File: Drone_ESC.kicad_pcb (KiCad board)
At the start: 2 copper layers, 62 parts, among them IC1 DRV8323RSRGZR, J1 Input, J2 62701021621, Q1 BSC014N06NS, Q2 BSC014N06NS, Q3 BSC014N06NS, Q4 BSC014N06NS, Q5 BSC014N06NS, Q6 BSC014N06NS, SW1 Reset, U1 STM32G473RCTx, Y1 XRCGB24M000F3A00R0

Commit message: Update Drone_ESC.kicad_pcb
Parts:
- C1, C10, C11, C12, C2, C21, C23, C24, C25, C26, C27, C28, C29, C3, C30, C31, C32, C4, C5, C6, C7, C8, C9, D1, IC1, R15, R16, U1: moved to B.Cu
- moved J2 147.4 mm to (130.9, 55.3)
- moved U1 135.9 mm to (142.5, 67.5), turned to 180 degrees
- moved R11 134.4 mm to (167.0, 67.5), turned to 180 degrees
- moved L1 131.0 mm to (142.1, 85.2)
- moved R12 130.4 mm to (167.0, 79.5), turned to 180 degrees
- moved IC1 129.8 mm to (153.0, 86.0), turned to -90 degrees
- moved D1 129.3 mm to (145.1, 85.8), turned to -90 degrees
- moved C5 128.2 mm to (132.3, 63.3), turned to -90 degrees
- moved C6 128.0 mm to (134.5, 63.3), turned to -90 degrees
- moved R13 126.6 mm to (167.0, 91.5), turned to 180 degrees
- moved C8 124.9 mm to (146.7, 59.5), turned to 180 degrees
- moved C7 124.5 mm to (146.7, 57.5), turned to 180 degrees
- moved R15 122.0 mm to (149.0, 77.8), turned to -90 degrees
- moved R16 121.8 mm to (151.0, 77.8), turned to 90 degrees
- moved C32 121.4 mm to (138.1, 83.0), turned to 90 degrees
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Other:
- copper layers 2 -> 6
- board text added: "1. Top: Main motor currents 2. GND 3. Critical Signals 4. 3.3V 5. Logic and BEMF 6. Leftover decoupling caps & GND pour"

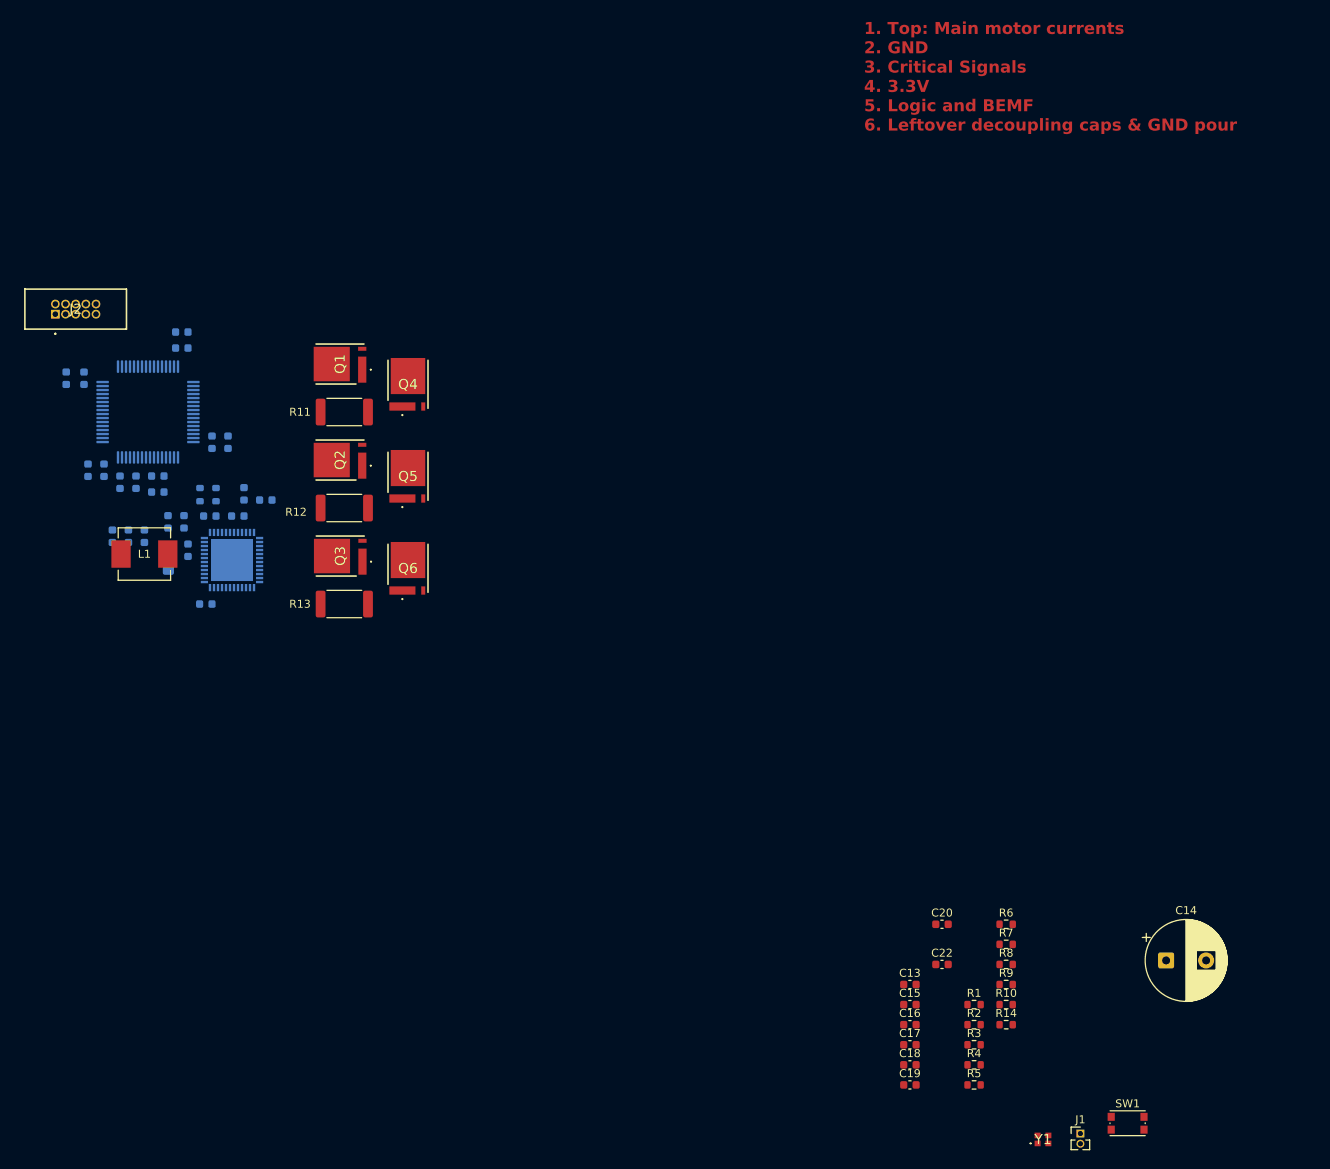
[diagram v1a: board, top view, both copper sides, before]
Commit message: PCB layout done, wiring next
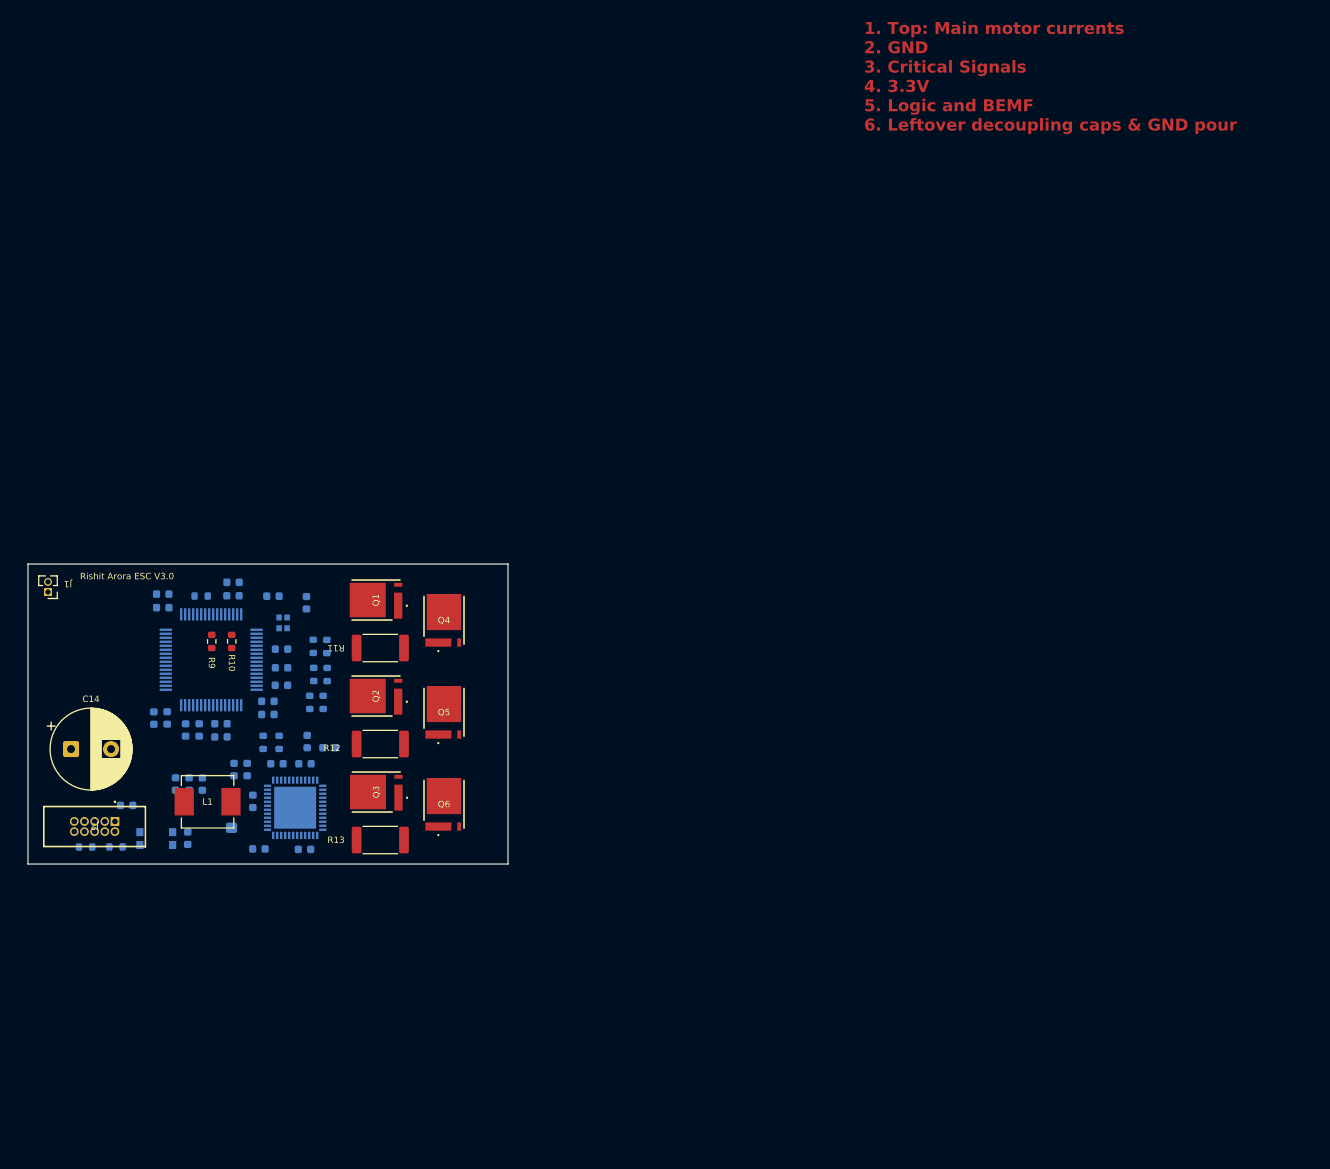
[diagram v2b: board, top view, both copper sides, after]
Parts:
- C13, C15, C16, C17, C18, C19, C20, C22, R1, R14, R2, R3, R4, R5, R6, R7, R8, SW1, Y1: moved to B.Cu
- moved J1 145.7 mm to (130.0, 90.0), turned to 180 degrees
- moved C14 139.4 mm to (132.9, 109.6)
- moved SW1 126.5 mm to (143.5, 120.8), turned to 180 degrees
- moved Y1 114.9 mm to (159.4, 93.9), turned to -90 degrees
- moved R14 114.0 mm to (149.1, 90.5), turned to 180 degrees
- moved R2 113.3 mm to (134.7, 121.9), turned to 180 degrees
- moved R1 109.1 mm to (138.5, 121.9), turned to 180 degrees
- moved R9 108.2 mm to (150.5, 96.2), turned to -90 degrees
- moved R10 106.9 mm to (153.0, 96.2), turned to -90 degrees
- moved C13 100.4 mm to (139.8, 116.7), turned to 180 degrees
- moved R3 95.0 mm to (164.9, 96.8), turned to 90 degrees
- moved R4 94.4 mm to (164.9, 100.3), turned to -90 degrees
- moved R5 94.4 mm to (164.4, 103.8), turned to -90 degrees
- moved R6 93.3 mm to (163.2, 96.8), turned to -90 degrees
- moved C20 93.1 mm to (158.1, 90.5)
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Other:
- board outline added: 60 x 37.5 mm
- board text added: "Rishit Arora ESC V3.0"

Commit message: Almost done with routing
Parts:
- moved C14 3.99 mm to (135.0, 106.2), turned to -90 degrees
- moved C22 1.74 mm to (163.8, 122.2)
- moved R9 1.56 mm to (151.7, 97.1)
- moved Q1 1.50 mm to (172.5, 91.0)
- moved Q2 1.50 mm to (172.5, 103.0)
- moved Q3 1.50 mm to (172.5, 115.0)
- moved Q4 1.50 mm to (181.0, 93.5)
- moved Q5 1.50 mm to (181.0, 105.0)
- moved Q6 1.50 mm to (181.0, 116.5)
- moved R11 1.50 mm to (173.0, 97.0)
- moved R12 1.50 mm to (173.0, 109.0)
- moved R13 1.50 mm to (173.0, 121.0)
- moved C28 1.24 mm to (161.7, 110.3)
- moved R10 1.19 mm to (154.1, 95.8)
- moved C24 0.82 mm to (155.3, 115.4)
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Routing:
- net RESET: track 0.00 -> 97.7 mm, vias 0 -> 2
- net GND: track 0.00 -> 96.2 mm, vias 0 -> 46
- net FAULT: track 0.00 -> 55.0 mm, vias 0 -> 3
- net +3.3V: track 0.00 -> 49.5 mm, vias 0 -> 16
- net SWO: track 0.00 -> 46.9 mm, vias 0 -> 1
- net SDO: track 0.00 -> 45.6 mm, vias 0 -> 2
- net DRIVER_EN: track 0.00 -> 43.0 mm, vias 0 -> 2
- net NSCS: track 0.00 -> 41.6 mm, vias 0 -> 2
- net SDI: track 0.00 -> 39.6 mm, vias 0 -> 2
- net SCLK: track 0.00 -> 39.0 mm, vias 0 -> 2
- net INHA: track 0.00 -> 37.9 mm, vias 0 -> 2
- net SWDCLK: track 0.00 -> 37.8 mm, vias 0 -> 1
- net INLA: track 0.00 -> 34.8 mm, vias 0 -> 2
- net INHC: track 0.00 -> 34.5 mm, vias 0 -> 2
- net INHB: track 0.00 -> 34.4 mm, vias 0 -> 2
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- added copper zone on B.Cu, net +3.3V
- added copper zone on F.Cu, net +3.3V
- added copper zone on In3.Cu, net +3.3V
- added copper zone on B.Cu, net +BATT
- added copper zone on F.Cu, net +BATT
- added copper zone on F.Cu, net GHA
- added copper zone on In2.Cu, net GHA
- added copper zone on F.Cu, net GHB
- added copper zone on In2.Cu, net GHB
- added copper zone on F.Cu, net GHC
- added copper zone on In2.Cu, net GHC
- added copper zone on F.Cu, net GLA
- added copper zone on In2.Cu, net GLA
- added copper zone on F.Cu, net GLB
- added copper zone on In2.Cu, net GLB
- added copper zone on F.Cu, net GLC
- added copper zone on In2.Cu, net GLC
- added copper zone on B.Cu, net GND
- added copper zone on In1.Cu, net GND
- added copper zone on B.Cu, net Net-(D1-K)
- added copper zone on B.Cu, net Net-(IC1-FB)
- added copper zone on F.Cu, net PHASE_A
- added copper zone on F.Cu, net PHASE_B
- added copper zone on F.Cu, net PHASE_C
- added copper zone on F.Cu, net SENSE_A
- added copper zone on F.Cu, net SENSE_B
- added copper zone on F.Cu, net SENSE_C
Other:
- board size 60 x 37.5 mm -> 64 x 38.5 mm

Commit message: Finished Routing everything
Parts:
- added J3: PWR, Drone_ESC_Local_Footprints:Power_Pads, F.Cu at (134.3, 96.5)
- added J4: Out_A, Drone_ESC_Local_Footprints:Motor_Pad, F.Cu at (187.4, 100.0)
- added J5: Out_B, Drone_ESC_Local_Footprints:Motor_Pad, F.Cu at (187.4, 111.7)
- added J6: Out_C, Drone_ESC_Local_Footprints:Motor_Pad, F.Cu at (187.4, 123.0)
- moved C14 1.41 mm to (136.3, 106.8), turned to 180 degrees
- moved J1 0.86 mm to (130.4, 89.2)
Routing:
- net GND: track 96.2 -> 175.4 mm, vias 46 -> 219
- net SOA: track 0.00 -> 37.4 mm, vias 0 -> 2
- net PHASE_B: track 0.00 -> 34.1 mm, vias 0 -> 4
- net SOB: track 0.00 -> 33.4 mm, vias 0 -> 2
- net SOC: track 0.00 -> 32.1 mm, vias 0 -> 2
- net PHASE_A: track 6.77 -> 38.6 mm, vias 1 -> 2
- net PHASE_C: track 0.00 -> 30.9 mm, vias 0 -> 3
- net GHB: track 0.00 -> 26.2 mm
- net SENSE_A: track 2.54 -> 25.0 mm, vias 0 -> 2
- net GLB: track 0.00 -> 21.6 mm, vias 1 -> 2
- net GLC: track 0.00 -> 19.5 mm
- net SENSE_B: track 0.00 -> 14.0 mm, vias 0 -> 2
- net SENSE_C: track 0.00 -> 12.9 mm, vias 0 -> 2
- net GHC: track 0.00 -> 12.5 mm
- net +3.3V: track 49.5 -> 52.6 mm
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- added copper zone on F.Cu, net GND
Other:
- outline, holes or cut-outs redrawn
